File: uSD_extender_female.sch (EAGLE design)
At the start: 5 parts

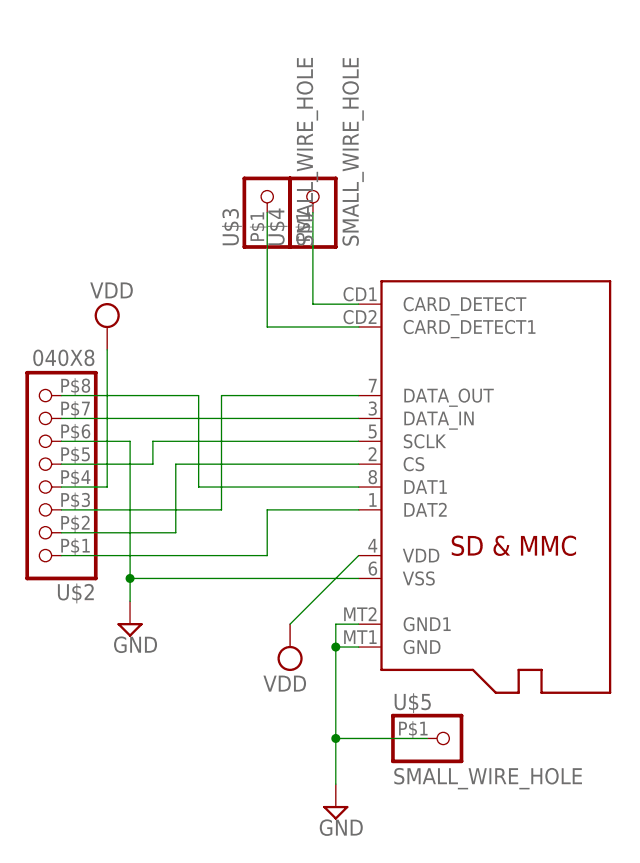
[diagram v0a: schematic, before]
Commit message: Update uSD_extender_female.sch
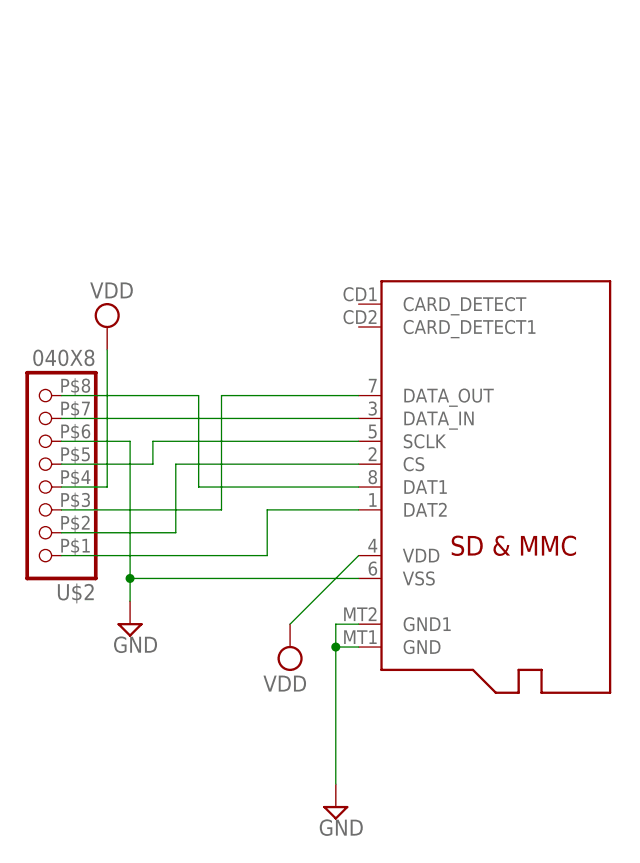
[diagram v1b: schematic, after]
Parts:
- removed U$3, U$4, U$5: SMALL_WIRE_HOLE, Dean:SMALL_WIRE_HOLE
- U$1: value MICROSD -> DEAN_MICROSD; device Dean:MICROSD -> uSD_extender_female:DEAN_MICROSD
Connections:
- removed net N$7: U$1.CARD_DETECT, U$4.1
- removed net N$8: U$1.CARD_DETECT1, U$3.1
- net GND: no longer U$5.1
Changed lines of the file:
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@@
 <?xml version="1.0" encoding="utf-8"?>
 <!DOCTYPE eagle SYSTEM "eagle.dtd">
-<eagle version="6.6.0">
+<eagle version="9.2.1">
 <drawing>
 <settings>
 <setting alwaysvectorfont="no"/>
+<setting keepoldvectorfont="yes"/>
 <setting verticaltext="up"/>
 </settings>
@@
 <layer number="2" name="Route2" color="1" fill="3" visible="no" active="no"/>
 <layer number="3" name="Route3" color="4" fill="3" visible="no" active="no"/>
+<layer number="4" name="Route4" color="1" fill="4" visible="no" active="no"/>
+<layer number="5" name="Route5" color="4" fill="4" visible="no" active="no"/>
+<layer number="6" name="Route6" color="1" fill="8" visible="no" active="no"/>
+<layer number="7" name="Route7" color="4" fill="8" visible="no" active="no"/>
+<layer number="8" name="Route8" color="1" fill="2" visible="no" active="no"/>
+<layer number="9" name="Route9" color="4" fill="2" visible="no" active="no"/>
+<layer number="10" name="Route10" color="1" fill="7" visible="no" active="no"/>
+<layer number="11" name="Route11" color="4" fill="7" visible="no" active="no"/>
+<layer number="12" name="Route12" color="1" fill="5" visible="no" active="no"/>
+<layer number="13" name="Route13" color="4" fill="5" visible="no" active="no"/>
 <layer number="14" name="Route14" color="1" fill="6" visible="no" active="no"/>
 <layer number="15" name="Route15" color="4" fill="6" visible="no" active="no"/>
@@
 <layer number="54" name="bGND_GNDA" color="1" fill="9" visible="no" active="no"/>
 <layer number="56" name="wert" color="7" fill="1" visible="no" active="no"/>
+<layer number="88" name="SimResults" color="9" fill="1" visible="yes" active="yes"/>
+<layer number="89" name="SimProbes" color="9" fill="1" visible="yes" active="yes"/>
+<layer number="90" name="Modules" color="5" fill="1" visible="yes" active="yes"/>
 <layer number="91" name="Nets" color="2" fill="1" visible="yes" active="yes"/>
 <layer number="92" name="Busses" color="1" fill="1" visible="yes" active="yes"/>
@@
 </classes>
 <parts>
-<part name="U$1" library="Dean" deviceset="MICROSD" device=""/>
+<part name="U$1" library="uSD_extender_female" library_urn="urn:adsk.eagle:library:5944486" deviceset="DEAN_MICROSD" device="" package3d_urn="urn:adsk.eagle:package:5944494/2"/>
 <part name="U$2" library="Dean" deviceset="040X8" device=""/>
-<part name="SUPPLY1" library="supply2" deviceset="GND" device=""/>
-<part name="SUPPLY2" library="supply2" deviceset="GND" device=""/>
-<part name="SUPPLY3" library="supply2" deviceset="VDD" device=""/>
-<part name="SUPPLY4" library="supply2" deviceset="VDD" device=""/>
-<part name="U$3" library="Dean" deviceset="SMALL_WIRE_HOLE" device=""/>
-<part name="U$4" library="Dean" deviceset="SMALL_WIRE_HOLE" device=""/>
-<part name="U$5" library="Dean" deviceset="SMALL_WIRE_HOLE" device=""/>
+<part name="SUPPLY1" library="supply2" library_urn="urn:adsk.eagle:library:372" deviceset="GND" device=""/>
+<part name="SUPPLY2" library="supply2" library_urn="urn:adsk.eagle:library:372" deviceset="GND" device=""/>
+<part name="SUPPLY3" library="supply2" library_urn="urn:adsk.eagle:library:372" deviceset="VDD" device=""/>
+<part name="SUPPLY4" library="supply2" library_urn="urn:adsk.eagle:library:372" deviceset="VDD" device=""/>
 </parts>
 <sheets>
@@
 </plain>
 <instances>
-<instance part="U$1" gate="G$1" x="55.88" y="33.02"/>
-<instance part="U$2" gate="G$1" x="2.54" y="30.48" rot="R180"/>
-<instance part="SUPPLY1" gate="GND" x="35.56" y="-5.08"/>
-<instance part="SUPPLY2" gate="GND" x="12.7" y="15.24"/>
-<instance part="SUPPLY3" gate="G$1" x="10.16" y="48.26"/>
-<instance part="SUPPLY4" gate="G$1" x="30.48" y="12.7" rot="R180"/>
-<instance part="U$3" gate="G$1" x="27.94" y="63.5" rot="R90"/>
-<instance part="U$4" gate="G$1" x="33.02" y="63.5" rot="R90"/>
-<instance part="U$5" gate="G$1" x="48.26" y="2.54"/>
+<instance part="U$1" gate="G$1" x="55.88" y="33.02" smashed="yes"/>
+<instance part="U$2" gate="G$1" x="2.54" y="30.48" smashed="yes" rot="R180">
+<attribute name="NAME" x="8.89" y="19.685" size="1.778" layer="95" rot="R180"/>
+<attribute name="VALUE" x="8.89" y="45.72" size="1.778" layer="96" rot="R180"/>
+</instance>
+<instance part="SUPPLY1" gate="GND" x="35.56" y="-5.08" smashed="yes">
+<attribute name="VALUE" x="33.655" y="-8.255" size="1.778" layer="96"/>
+</instance>
+<instance part="SUPPLY2" gate="GND" x="12.7" y="15.24" smashed="yes">
+<attribute name="VALUE" x="10.795" y="12.065" size="1.778" layer="96"/>
+</instance>
+<instance part="SUPPLY3" gate="G$1" x="10.16" y="48.26" smashed="yes">
+<attribute name="VALUE" x="8.255" y="51.435" size="1.778" layer="96"/>
+</instance>
+<instance part="SUPPLY4" gate="G$1" x="30.48" y="12.7" smashed="yes" rot="R180">
+<attribute name="VALUE" x="32.385" y="9.525" size="1.778" layer="96" rot="R180"/>
+</instance>
 </instances>
 <busses>
@@
 <wire x1="35.56" y1="15.24" x2="35.56" y2="12.7" width="0.1524" layer="91"/>
 <pinref part="U$1" gate="G$1" pin="GND"/>
-<wire x1="35.56" y1="12.7" x2="35.56" y2="2.54" width="0.1524" layer="91"/>
-<wire x1="35.56" y1="2.54" x2="35.56" y2="-2.54" width="0.1524" layer="91"/>
+<wire x1="35.56" y1="12.7" x2="35.56" y2="-2.54" width="0.1524" layer="91"/>
 <wire x1="38.1" y1="12.7" x2="35.56" y2="12.7" width="0.1524" layer="91"/>
-<pinref part="U$5" gate="G$1" pin="1"/>
-<wire x1="45.72" y1="2.54" x2="35.56" y2="2.54" width="0.1524" layer="91"/>
-<junction x="35.56" y="2.54"/>
 <junction x="35.56" y="12.7"/>
 </segment>
@@
 </segment>
 </net>
-<net name="N$7" class="0">
-<segment>
-<pinref part="U$4" gate="G$1" pin="1"/>
-<wire x1="33.02" y1="60.96" x2="33.02" y2="50.8" width="0.1524" layer="91"/>
-<pinref part="U$1" gate="G$1" pin="CARD_DETECT"/>
-<wire x1="33.02" y1="50.8" x2="38.1" y2="50.8" width="0.1524" layer="91"/>
-</segment>
-</net>
-<net name="N$8" class="0">
-<segment>
-<pinref part="U$3" gate="G$1" pin="1"/>
-<wire x1="27.94" y1="60.96" x2="27.94" y2="48.26" width="0.1524" layer="91"/>
-<pinref part="U$1" gate="G$1" pin="CARD_DETECT1"/>
-<wire x1="27.94" y1="48.26" x2="38.1" y2="48.26" width="0.1524" layer="91"/>
-</segment>
-</net>
 </nets>
 </sheet>
@@
 </schematic>
 </drawing>
+<compatibility>
+<note version="8.2" severity="warning">
+Since Version 8.2, EAGLE supports online libraries. The ids
+of those online libraries will not be understood (or retained)
+with this version.
+</note>
+<note version="8.3" severity="warning">
+Since Version 8.3, EAGLE supports URNs for individual library
+assets (packages, symbols, and devices). The URNs of those assets
+will not be understood (or retained) with this version.
+</note>
+<note version="8.3" severity="warning">
+Since Version 8.3, EAGLE supports the association of 3D packages
+with devices in libraries, schematics, and board files. Those 3D
+packages will not be understood (or retained) with this version.
+</note>
+</compatibility>
 </eagle>
